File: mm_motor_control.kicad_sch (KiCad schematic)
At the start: 0 parts

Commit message: tp2
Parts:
- added C18: 22uF 16V, symbol Device:C_Polarized
- added C7: 22nF, symbol Device:C_Small
- added C7: 1nF 6.3V, symbol Device:C_Small
- added C7: 2.2uF 16V, symbol Device:C_Small
- added C7: 10nF 6.3V, symbol Device:C_Small
- added R10, R11, R13, R18: 18k, symbol Device:R_Small
- added R14, R15: 10k, symbol Device:R_Small
- added R16: 1k, symbol Device:R_Small
- added R17: 47k, symbol Device:R_Small
- added U3: STSPIN240, symbol minimouse_yousfi_sym:STSPIN240
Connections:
- net EN: now also R18.1
- net FAULT: now also C7.1, R18.2, U3.13 (EN\FAULT)
- net OUT_A1: now also U3.3 (OUTA1)
- net OUT_A2: now also U3.5 (OUTA2)
- net OUT_B1: now also U3.10 (OUTB1)
- net OUT_B2: now also U3.8 (OUTB2)
- net PHASE_A: now also U3.1 (PHA)
- net PHASE_B: now also U3.15 (PHB)
- net PWM_A: now also U3.2 (PWMA)
- net PWM_B: now also U3.16 (PWMB)
- net STBY/RESET: now also C7.1, R10.2, U3.14 (STBY\RESET)
- new net: C7.1, R16.2
- new net: R13.1, U3.4 (SENSEA)
- new net: R11.1, U3.9 (SENSEB)
- new net +3.3V: R10.1
- new net +BATT: C18.1, C7.1, R14.1, U3.6 (VS)
- new net GND: C18.2, C7.2, C7.2, C7.2, C7.2, R11.2, R13.2, R15.2, R17.2, U3.17 (EPAD), U3.7 (GND)
- new net REF: R14.2, R15.1, U3.11 (REF)
- new net TOFF: R16.1, R17.1, U3.12 (TOFF)

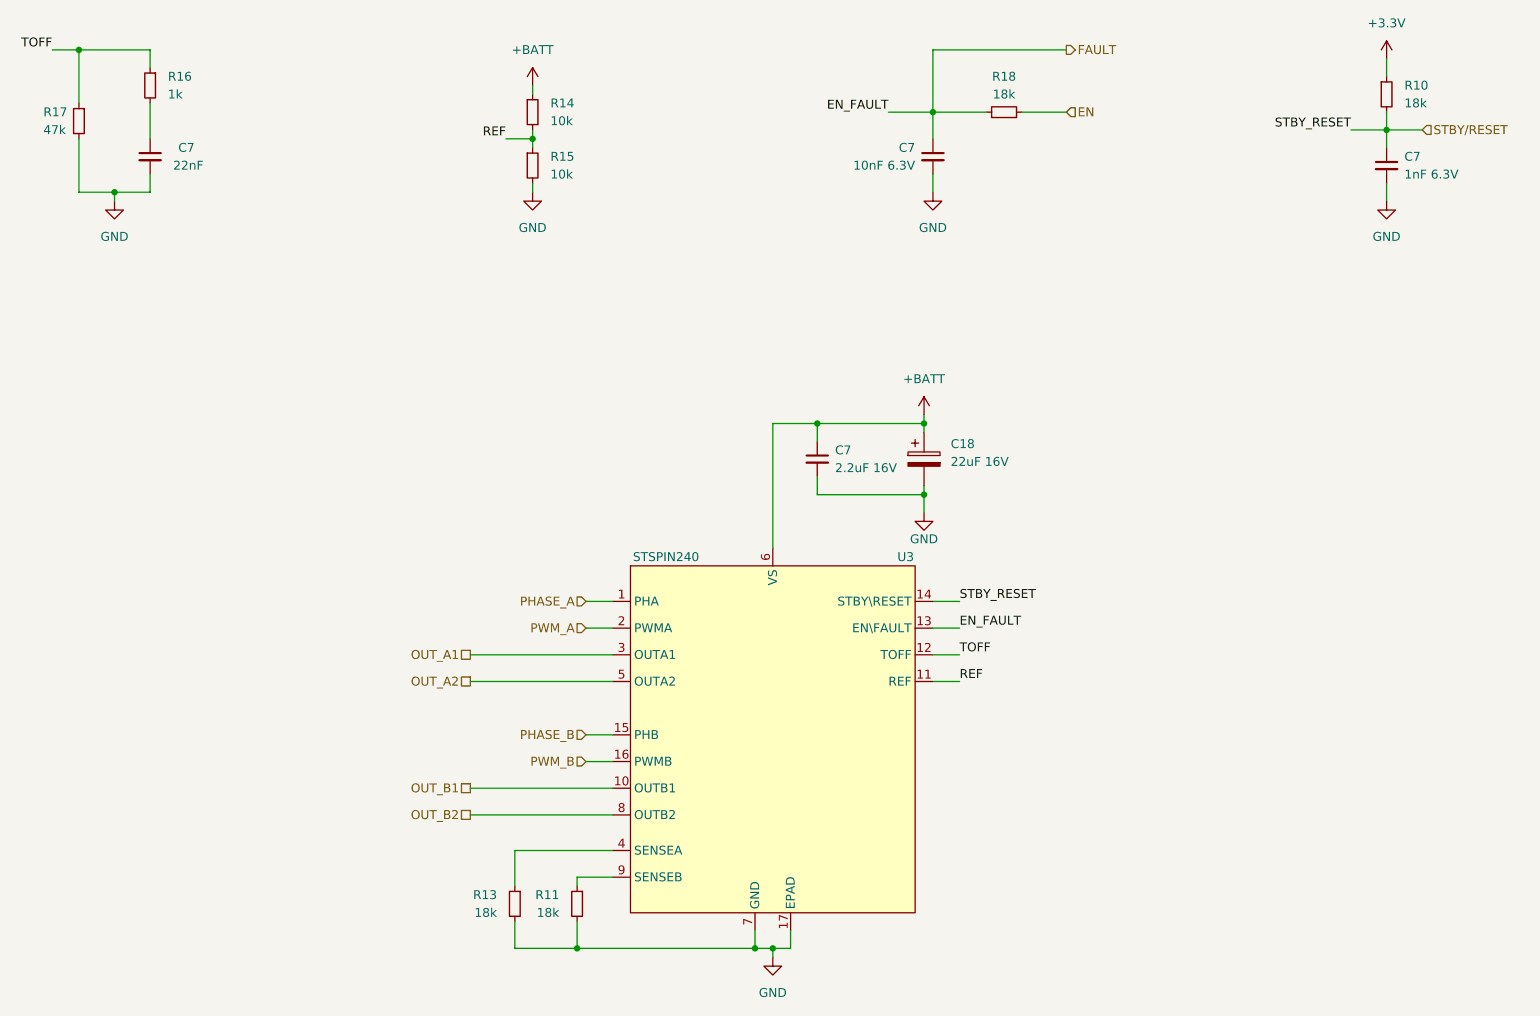
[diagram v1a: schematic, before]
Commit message: updated to kicad 8.0
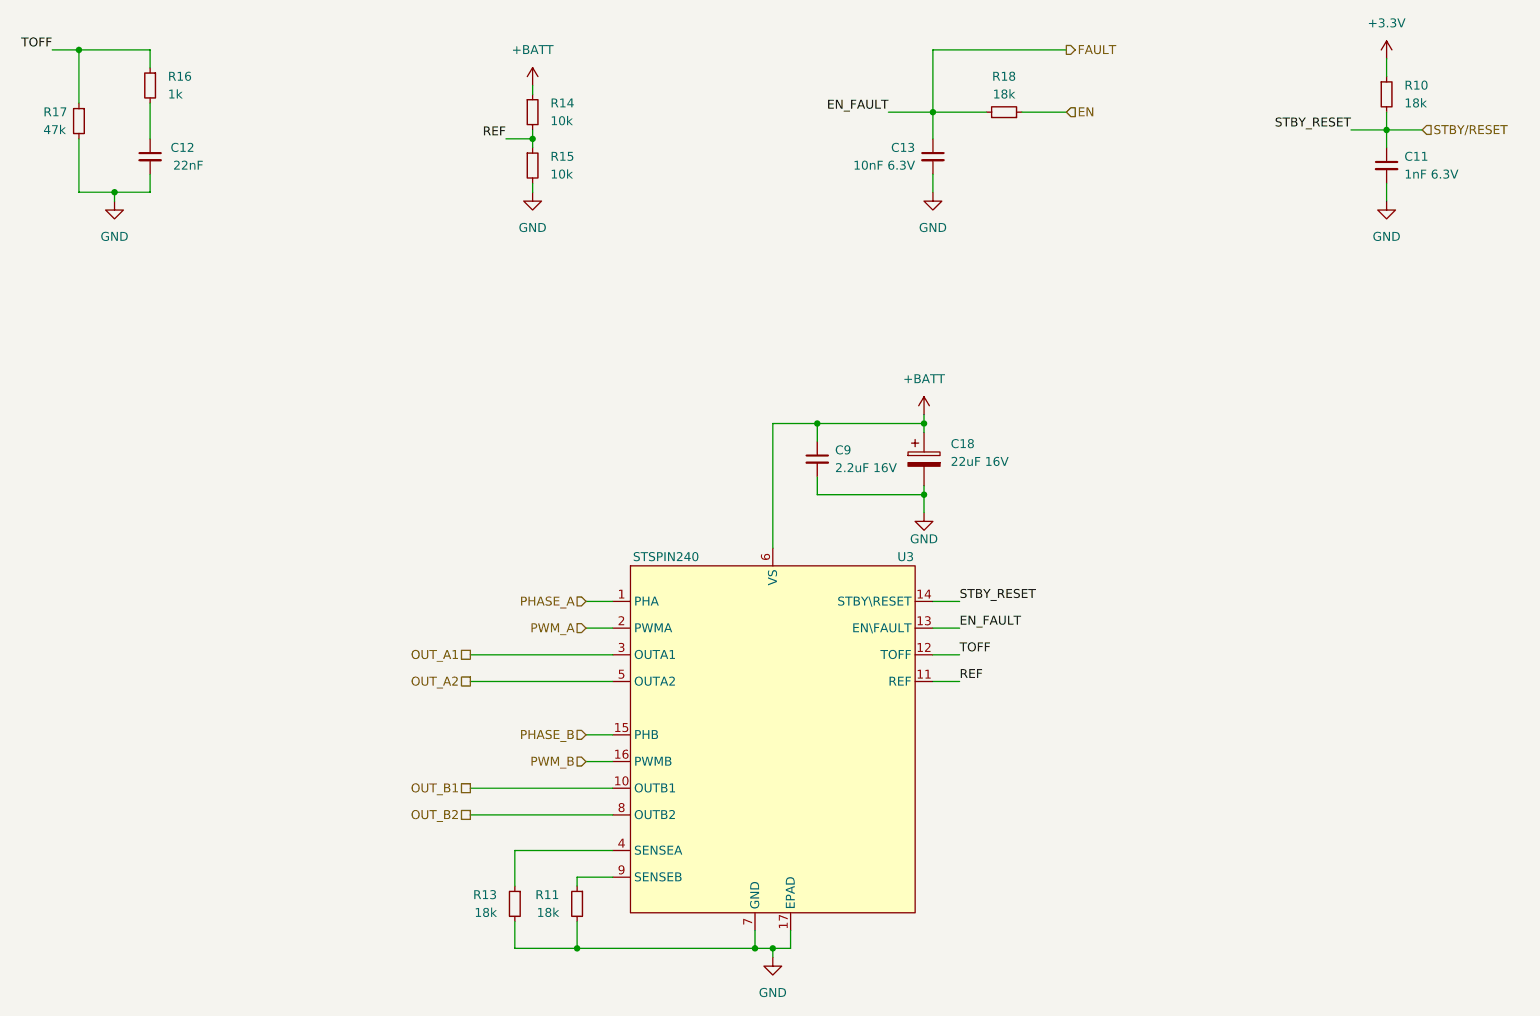
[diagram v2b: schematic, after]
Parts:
- renumbered C7 to C11, C7 to C12, C7 to C13, C7 to C9
